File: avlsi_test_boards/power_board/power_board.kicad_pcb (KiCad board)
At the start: 4 copper layers, 99.9 x 100 mm, 100 parts, among them J1 2171750001, J2 2171750001, J3 Conn_01x02_Pin, J4 Conn_01x02_Pin, J5 Conn_01x02_Pin, J6 Conn_01x02_Pin, U1 TLV75709PDBV, U10 TLV1117LV33DCYR, U13 SN74LVC16T245DLR, U14 SN74LVC16T245DLR, U15 SN74LVC16T245DLR, U16 SN74LVC16T245DLR, U17 SN74LVC16T245DLR, U18 SN74LVC16T245DLR, U2 TLV1117LV18DCYR, U3 TLV1117LV25DCYR, U4 TLV1117LV33DCYR, U5 DS04-254-2-04BK-SMT, U6 74HC4051D_653, U7 TLV1117LV18DCYR, U8 TLV75709PDBV, U9 TLV1117LV25DCYR

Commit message: Add production files
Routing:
- net DGND: track 100.2 -> 383.9 mm, vias 92 -> 95
- net DVIN5: track 168.2 -> 171.3 mm, vias 14 -> 12
- net V_Level_Shift: track 88.1 -> 90.4 mm
- net /level_shifters/LS9_DIR1: track 31.3 -> 32.8 mm
- net /level_shifters/LS11_DIR2: track 26.3 -> 25.3 mm
- net MC2_45: track 29.7 -> 28.8 mm
- net MC2_54: track 70.2 -> 70.0 mm, vias 2 -> 1
- net unconnected-(U12B-SYS_CLK_MC2-Pad91): vias 1 -> 0
- net unconnected-(U12B-MC2_73-Pad153): vias 1 -> 0
- net unconnected-(U12B-MC2_71-Pad151): vias 1 -> 0
- net unconnected-(U12B-MC2_69-Pad149): vias 1 -> 0
- net unconnected-(U12B-MC2_67-Pad147): vias 1 -> 0
- net unconnected-(U12B-MC2_65-Pad145): vias 1 -> 0
- net unconnected-(U12B-MC2_63-Pad143): vias 1 -> 0
- net unconnected-(U12B-MC2_61-Pad141): vias 1 -> 0
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
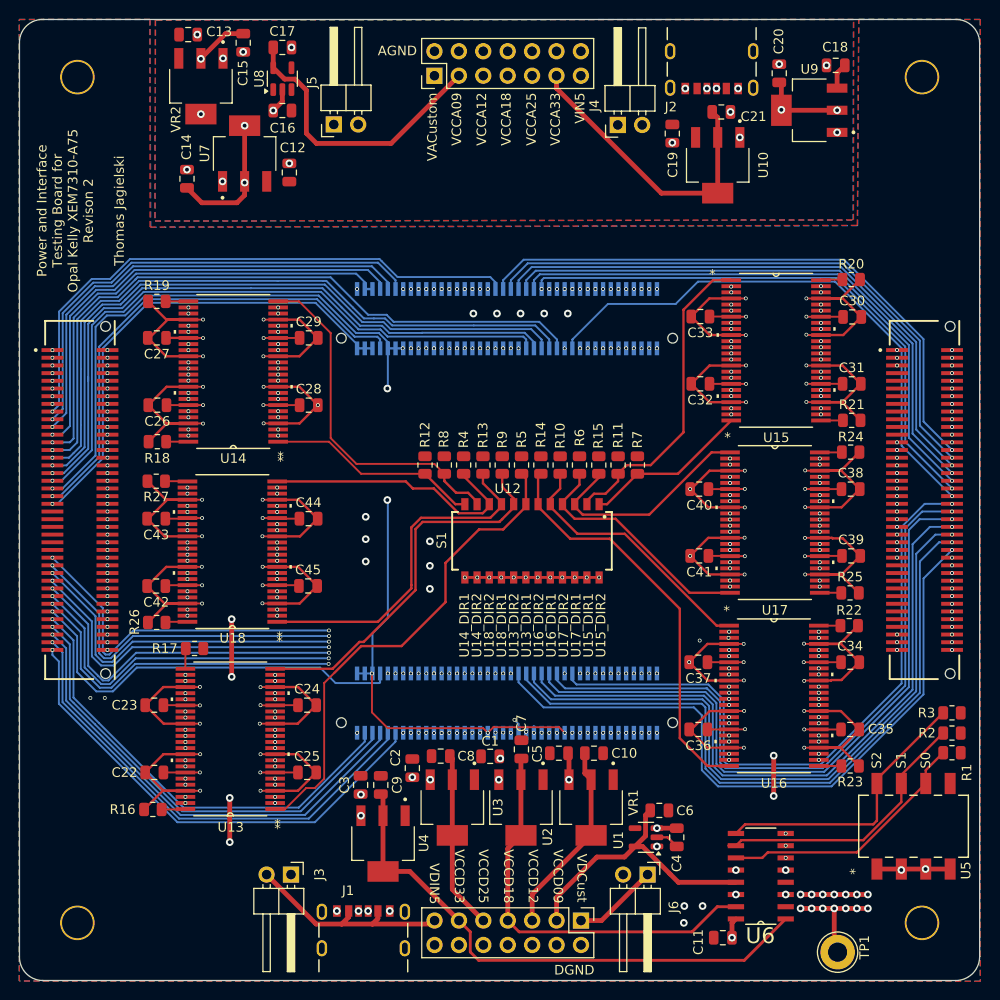
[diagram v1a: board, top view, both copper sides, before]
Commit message: Add power board
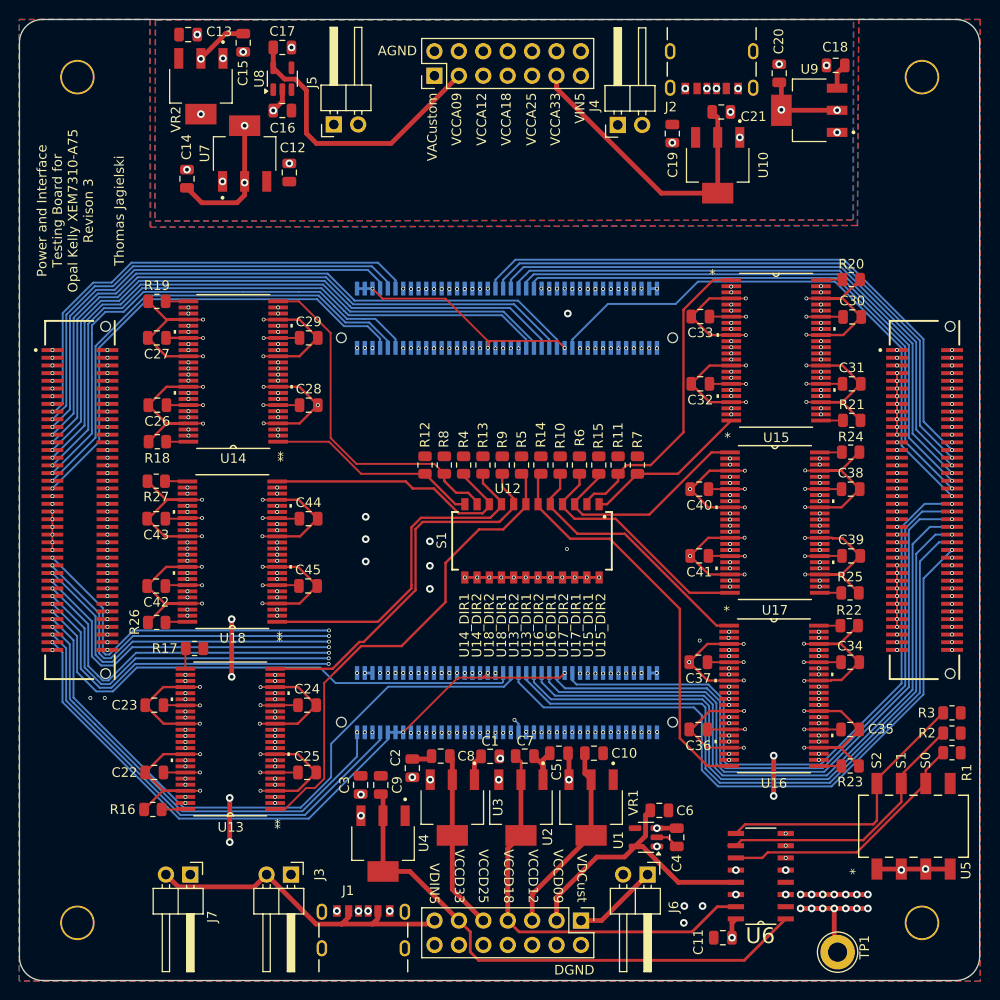
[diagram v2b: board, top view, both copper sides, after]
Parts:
- added J7: Conn_01x02_Pin, Connector_PinHeader_2.54mm:PinHeader_1x02_P2.54mm_Horizontal, F.Cu at (117.9, 114.4)
- moved C7 0.78 mm to (152.7, 102.0), turned to 0 degrees
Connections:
- net MC1_32_PIN renamed MC2_32_PIN
- net MC1_34_PIN renamed MC2_34_PIN
- net MC1_50_PIN renamed MC2_50_PIN
- net MC1_52_PIN renamed MC2_52_PIN
- net MC1_54_PIN renamed MC2_54_PIN
- net MC1_58_PIN renamed MC2_58_PIN
- net MC2_45_PIN renamed MC1_45_PIN
- net MC2_47_PIN renamed MC1_47_PIN
- net MC2_49_PIN renamed MC1_49_PIN
- net MC2_51_PIN renamed MC1_51_PIN
- net MC2_53_PIN renamed MC1_53_PIN
- net MC2_57_PIN renamed MC1_57_PIN
- U12 pad 01: MC1_16_PIN -> MC2_16_PIN
- U12 pad 03: MC1_18_PIN -> MC2_18_PIN
- U12 pad 05: MC1_20_PIN -> MC2_20_PIN
- U12 pad 06: MC1_15_PIN -> MC2_15_PIN
- U12 pad 07: MC1_22_PIN -> MC2_22_PIN
- U12 pad 08: MC1_17_PIN -> MC2_17_PIN
- U12 pad 09: MC1_24_PIN -> MC2_24_PIN
- U12 pad 10: MC1_19_PIN -> MC2_19_PIN
- U12 pad 101: unconnected-(U12B-MC2_21-Pad101) -> DGND
- U12 pad 103: unconnected-(U12B-MC2_23-Pad103) -> DGND
- U12 pad 105: MC1_73_PIN -> MC2_73_PIN
- U12 pad 107: MC1_71_PIN -> MC2_71_PIN
- U12 pad 108: MC1_40 -> MC2_38
- U12 pad 109: MC1_69_PIN -> MC2_69_PIN
- U12 pad 11: MC1_26_PIN -> MC2_26_PIN
- U12 pad 110: MC1_42 -> MC2_40
- U12 pad 111: MC1_67_PIN -> MC2_67_PIN
- U12 pad 112: MC1_44 -> MC2_42
- U12 pad 113: MC1_65_PIN -> MC2_65_PIN
- U12 pad 114: MC1_46 -> MC2_44
- U12 pad 115: MC1_63_PIN -> MC2_63_PIN
- U12 pad 116: MC1_48 -> MC2_46
- U12 pad 117: MC1_61_PIN -> MC2_61_PIN
- U12 pad 118: MC1_50 -> MC2_48
- U12 pad 119: MC1_59_PIN -> MC2_59_PIN
- U12 pad 12: MC1_21_PIN -> MC2_21_PIN
- U12 pad 120: MC1_57 -> MC2_57
- U12 pad 121: MC2_60_PIN -> MC1_60_PIN
- U12 pad 122: MC2_58 -> MC1_58
- U12 pad 123: MC2_62_PIN -> MC1_62_PIN
- U12 pad 124: MC2_54 -> MC1_54
- U12 pad 125: MC2_64_PIN -> MC1_64_PIN
- U12 pad 126: MC2_52 -> MC1_52
- U12 pad 127: MC2_66_PIN -> MC1_66_PIN
- U12 pad 128: MC2_50 -> MC1_50
- U12 pad 129: MC2_68_PIN -> MC1_68_PIN
- U12 pad 13: MC1_28_PIN -> MC2_28_PIN
- U12 pad 130: MC2_48 -> MC1_48
- U12 pad 131: MC2_70_PIN -> MC1_70_PIN
- U12 pad 132: MC2_46 -> MC1_46
- U12 pad 133: MC2_72_PIN -> MC1_72_PIN
- U12 pad 134: MC2_44 -> MC1_44
- U12 pad 135: MC2_74_PIN -> MC1_74_PIN
- U12 pad 136: MC2_67_PIN -> MC1_67_PIN
- U12 pad 137: unconnected-(U12B-MC2_57-Pad137) -> DGND
- U12 pad 138: MC2_69_PIN -> MC1_69_PIN
- U12 pad 139: unconnected-(U12B-MC2_59-Pad139) -> DGND
- U12 pad 14: MC1_23_PIN -> MC2_23_PIN
- U12 pad 140: MC2_71_PIN -> MC1_71_PIN
- U12 pad 141: unconnected-(U12B-MC2_61-Pad141) -> DGND
- U12 pad 142: MC2_73_PIN -> MC1_73_PIN
- U12 pad 143: unconnected-(U12B-MC2_63-Pad143) -> DGND
- U12 pad 144: MC2_75_PIN -> MC1_75_PIN
- U12 pad 145: unconnected-(U12B-MC2_65-Pad145) -> DGND
- U12 pad 146: MC2_77_PIN -> MC1_77_PIN
- U12 pad 147: unconnected-(U12B-MC2_67-Pad147) -> DGND
- U12 pad 148: MC2_79_PIN -> MC1_79_PIN
- U12 pad 149: unconnected-(U12B-MC2_69-Pad149) -> DGND
- U12 pad 15: MC1_30_PIN -> MC2_30_PIN
- U12 pad 150: MC2_61_PIN -> MC1_61_PIN
- U12 pad 151: unconnected-(U12B-MC2_71-Pad151) -> DGND
- U12 pad 152: MC2_59_PIN -> MC1_59_PIN
- U12 pad 153: unconnected-(U12B-MC2_73-Pad153) -> DGND
- U12 pad 155: MC2_76_PIN -> MC1_76_PIN
- U12 pad 157: MC2_63_PIN -> MC1_63_PIN
- U12 pad 159: MC2_65_PIN -> MC1_65_PIN
- U12 pad 16: MC1_25_PIN -> MC2_25_PIN
- U12 pad 17: MC1_38 -> MC2_12
- U12 pad 18: MC1_27_PIN -> MC2_27_PIN
- U12 pad 19: XADC_VP -> MC2_10
- U12 pad 20: MC1_29_PIN -> MC2_29_PIN
- U12 pad 21: XADC_VN -> FPGA_TDO
- U12 pad 22: MC1_31_PIN -> MC2_31_PIN
- U12 pad 23: SYS_CLK_MC1 -> MC2_53
- U12 pad 24: MC1_33_PIN -> MC2_33_PIN
- U12 pad 25: FPGA_10VDD -> MC2_51
- U12 pad 26: MC1_37_PIN -> MC2_37_PIN
- U12 pad 27: MC1_53 -> MC2_49
- U12 pad 28: MC1_39_PIN -> MC2_39_PIN
- U12 pad 29: MC1_51 -> MC2_47
- U12 pad 30: MC1_41_PIN -> MC2_41_PIN
- U12 pad 31: MC1_49 -> MC2_45
- U12 pad 32: MC1_43_PIN -> MC2_43_PIN
- U12 pad 33: MC1_47 -> SYS_CLK_MC2
- U12 pad 34: MC2_26_PIN -> MC1_30_PIN
- U12 pad 35: MC1_45 -> FPGA_TDI
- U12 pad 36: MC2_24_PIN -> MC1_28_PIN
- U12 pad 37: FPGA_33VDD -> FPGA_TMS
- U12 pad 38: MC2_22_PIN -> MC1_26_PIN
- U12 pad 39: FPGA_18VDD -> FPGA_TCK
- U12 pad 40: MC2_20_PIN -> MC1_24_PIN
- U12 pad 41: FPGA_VCDIN -> VCCBATT
- U12 pad 42: MC2_18_PIN -> MC1_22_PIN
- U12 pad 43: unconnected-(U12A-MC1_43-Pad43) -> DGND
- U12 pad 44: MC2_16_PIN -> MC1_20_PIN
- U12 pad 45: unconnected-(U12A-MC1_45-Pad45) -> DGND
- U12 pad 46: MC2_12_PIN -> MC1_18_PIN
- U12 pad 47: unconnected-(U12A-MC1_47-Pad47) -> DGND
- U12 pad 48: MC2_10_PIN -> MC1_16_PIN
- U12 pad 49: unconnected-(U12A-MC1_49-Pad49) -> DGND
- U12 pad 51: unconnected-(U12A-MC1_51-Pad51) -> DGND
- U12 pad 53: unconnected-(U12A-MC1_53-Pad53) -> DGND
- U12 pad 54: MC2_43_PIN -> MC1_43_PIN
- U12 pad 55: MC2_42 -> MC1_38
- U12 pad 56: MC2_41_PIN -> MC1_41_PIN
- U12 pad 57: MC2_40 -> MC1_34
- U12 pad 58: MC2_39_PIN -> MC1_39_PIN
- U12 pad 59: MC2_38 -> MC1_32
- U12 pad 60: MC2_37_PIN -> MC1_37_PIN
- U12 pad 61: MC2_34 -> XADC_VP
- U12 pad 62: MC2_33_PIN -> MC1_33_PIN
- U12 pad 63: MC2_32 -> XADC_VN
- U12 pad 64: MC2_31_PIN -> MC1_31_PIN
- U12 pad 65: MC2_30 -> SYS_CLK_MC1
- U12 pad 66: MC2_15_PIN -> MC1_15_PIN
- U12 pad 67: MC2_28 -> FPGA_10VDD
- U12 pad 68: MC2_17_PIN -> MC1_17_PIN
- U12 pad 69: FPGA_TDO -> MC1_40
- U12 pad 70: MC2_19_PIN -> MC1_19_PIN
- U12 pad 71: VCCBATT -> MC1_42
- U12 pad 72: MC2_21_PIN -> MC1_21_PIN
- U12 pad 73: FPGA_TCK -> FPGA_VCDIN
- U12 pad 74: MC2_23_PIN -> MC1_23_PIN
- U12 pad 75: FPGA_TMS -> FPGA_18VDD
- U12 pad 76: MC2_25_PIN -> MC1_25_PIN
- U12 pad 77: FPGA_TDI -> FPGA_33VDD
- U12 pad 78: MC2_27_PIN -> MC1_27_PIN
- U12 pad 79: SYS_CLK_MC2 -> DGND
- U12 pad 80: MC2_29_PIN -> MC1_29_PIN
- U12 pad 81: MC1_79_PIN -> MC2_79_PIN
- U12 pad 82: MC1_68_PIN -> MC2_68_PIN
- U12 pad 83: MC1_77_PIN -> MC2_77_PIN
- U12 pad 84: MC1_70_PIN -> MC2_70_PIN
- U12 pad 85: MC1_75_PIN -> MC2_75_PIN
- U12 pad 86: MC1_72_PIN -> MC2_72_PIN
- U12 pad 87: unconnected-(U12B-FPGA_TMS-Pad87) -> DGND
- U12 pad 88: MC1_76_PIN -> MC2_76_PIN
- U12 pad 89: unconnected-(U12B-FPGA_TDI-Pad89) -> DGND
- U12 pad 90: MC1_74_PIN -> MC2_74_PIN
- U12 pad 91: unconnected-(U12B-SYS_CLK_MC2-Pad91) -> DGND
- U12 pad 92: MC1_66_PIN -> MC2_66_PIN
- U12 pad 93: unconnected-(U12B-DGND-Pad93) -> DGND
- U12 pad 94: MC1_64_PIN -> MC2_64_PIN
- U12 pad 95: unconnected-(U12B-MC2_15-Pad95) -> DGND
- U12 pad 96: MC1_62_PIN -> MC2_62_PIN
- U12 pad 97: unconnected-(U12B-MC2_17-Pad97) -> DGND
- U12 pad 98: MC1_60_PIN -> MC2_60_PIN
- U12 pad 99: unconnected-(U12B-MC2_19-Pad99) -> DGND
- U13 pad 11: MC2_17 -> MC1_17
- U13 pad 12: MC2_15 -> MC1_15
- U13 pad 13: MC2_31 -> MC1_31
- U13 pad 14: MC2_33 -> MC1_33
- U13 pad 16: MC2_37 -> MC1_37
- U13 pad 17: MC2_39 -> MC1_39
- U13 pad 19: MC2_41 -> MC1_41
- U13 pad 2: MC2_29 -> MC1_29
- U13 pad 20: MC2_43 -> MC1_43
- U13 pad 22: MC2_45 -> MC1_45
- U13 pad 23: MC2_47 -> MC1_47
- U13 pad 29: MC2_43_PIN -> MC1_43_PIN
- U13 pad 3: MC2_27 -> MC1_27
- U13 pad 30: MC2_41_PIN -> MC1_41_PIN
- U13 pad 32: MC2_39_PIN -> MC1_39_PIN
- U13 pad 33: MC2_37_PIN -> MC1_37_PIN
- U13 pad 35: MC2_33_PIN -> MC1_33_PIN
- U13 pad 36: MC2_31_PIN -> MC1_31_PIN
- U13 pad 37: MC2_15_PIN -> MC1_15_PIN
- U13 pad 38: MC2_17_PIN -> MC1_17_PIN
- U13 pad 40: MC2_19_PIN -> MC1_19_PIN
- U13 pad 41: MC2_21_PIN -> MC1_21_PIN
- U13 pad 43: MC2_23_PIN -> MC1_23_PIN
- U13 pad 44: MC2_25_PIN -> MC1_25_PIN
- U13 pad 46: MC2_27_PIN -> MC1_27_PIN
- U13 pad 47: MC2_29_PIN -> MC1_29_PIN
- U13 pad 5: MC2_25 -> MC1_25
- U13 pad 6: MC2_23 -> MC1_23
- U13 pad 8: MC2_21 -> MC1_21
- U13 pad 9: MC2_19 -> MC1_19
- U14 pad 11: MC1_34 -> MC2_34
- U14 pad 12: MC1_32 -> MC2_32
- U14 pad 13: MC1_30 -> MC2_30
- U14 pad 14: MC1_28 -> MC2_28
- U14 pad 16: MC1_26 -> MC2_26
- U14 pad 17: MC1_24 -> MC2_24
- U14 pad 19: MC1_22 -> MC2_22
- U14 pad 2: MC1_25 -> MC2_25
- U14 pad 20: MC1_20 -> MC2_20
- U14 pad 22: MC1_18 -> MC2_18
- U14 pad 23: MC1_16 -> MC2_16
- U14 pad 26: MC1_16_PIN -> MC2_16_PIN
- U14 pad 27: MC1_18_PIN -> MC2_18_PIN
- U14 pad 29: MC1_20_PIN -> MC2_20_PIN
- U14 pad 3: MC1_23 -> MC2_23
- U14 pad 30: MC1_22_PIN -> MC2_22_PIN
- U14 pad 32: MC1_24_PIN -> MC2_24_PIN
- U14 pad 33: MC1_26_PIN -> MC2_26_PIN
- U14 pad 35: MC1_28_PIN -> MC2_28_PIN
- U14 pad 36: MC1_30_PIN -> MC2_30_PIN
- U14 pad 40: MC1_15_PIN -> MC2_15_PIN
- U14 pad 41: MC1_17_PIN -> MC2_17_PIN
- U14 pad 43: MC1_19_PIN -> MC2_19_PIN
- U14 pad 44: MC1_21_PIN -> MC2_21_PIN
- U14 pad 46: MC1_23_PIN -> MC2_23_PIN
- U14 pad 47: MC1_25_PIN -> MC2_25_PIN
- U14 pad 5: MC1_21 -> MC2_21
- U14 pad 6: MC1_19 -> MC2_19
- U14 pad 8: MC1_17 -> MC2_17
- U14 pad 9: MC1_15 -> MC2_15
- U15 pad 11: MC1_64 -> MC2_64
- U15 pad 12: MC1_62 -> MC2_62
- U15 pad 13: MC1_60 -> MC2_60
- U15 pad 14: MC1_58 -> MC2_58
- U15 pad 16: MC1_54 -> MC2_54
- U15 pad 17: MC1_52 -> MC2_52
- U15 pad 19: MC1_50 -> MC2_50
- U15 pad 2: MC1_74 -> MC2_74
- U15 pad 20: MC1_79 -> MC2_79
- U15 pad 22: MC1_77 -> MC2_77
- U15 pad 23: MC1_75 -> MC2_75
- U15 pad 26: MC1_75_PIN -> MC2_75_PIN
- U15 pad 27: MC1_77_PIN -> MC2_77_PIN
- U15 pad 29: MC1_79_PIN -> MC2_79_PIN
- U15 pad 3: MC1_76 -> MC2_76
- U15 pad 36: MC1_60_PIN -> MC2_60_PIN
- U15 pad 37: MC1_62_PIN -> MC2_62_PIN
- U15 pad 38: MC1_64_PIN -> MC2_64_PIN
- U15 pad 40: MC1_66_PIN -> MC2_66_PIN
- U15 pad 41: MC1_68_PIN -> MC2_68_PIN
- U15 pad 43: MC1_70_PIN -> MC2_70_PIN
- U15 pad 44: MC1_72_PIN -> MC2_72_PIN
- U15 pad 46: MC1_76_PIN -> MC2_76_PIN
- U15 pad 47: MC1_74_PIN -> MC2_74_PIN
- U15 pad 5: MC1_72 -> MC2_72
- U15 pad 6: MC1_70 -> MC2_70
- U15 pad 8: MC1_68 -> MC2_68
- U15 pad 9: MC1_66 -> MC2_66
- U16 pad 11: MC2_73 -> MC1_73
- U16 pad 12: MC2_75 -> MC1_75
- U16 pad 13: MC2_77 -> MC1_79
- U16 pad 14: MC2_79 -> MC1_77
- U16 pad 16: MC2_61 -> MC1_61
- U16 pad 17: MC2_59 -> MC1_59
- U16 pad 19: MC2_57 -> MC1_57
- U16 pad 2: MC2_76 -> MC1_76
- U16 pad 20: MC2_53 -> MC1_53
- U16 pad 22: MC2_51 -> MC1_51
- U16 pad 23: MC2_49 -> MC1_49
- U16 pad 3: MC2_63 -> MC1_63
- U16 pad 32: MC2_59_PIN -> MC1_59_PIN
- U16 pad 33: MC2_61_PIN -> MC1_61_PIN
- U16 pad 35: MC2_79_PIN -> MC1_79_PIN
- U16 pad 36: MC2_77_PIN -> MC1_77_PIN
- U16 pad 37: MC2_75_PIN -> MC1_75_PIN
- U16 pad 38: MC2_73_PIN -> MC1_73_PIN
- U16 pad 40: MC2_71_PIN -> MC1_71_PIN
- U16 pad 41: MC2_69_PIN -> MC1_69_PIN
- U16 pad 43: MC2_67_PIN -> MC1_67_PIN
- U16 pad 44: MC2_65_PIN -> MC1_65_PIN
- U16 pad 46: MC2_63_PIN -> MC1_63_PIN
- U16 pad 47: MC2_76_PIN -> MC1_76_PIN
- U16 pad 5: MC2_65 -> MC1_65
- U16 pad 6: MC2_67 -> MC1_67
- U16 pad 8: MC2_69 -> MC1_69
- U16 pad 9: MC2_71 -> MC1_71
- U17 pad 11: MC1_61 -> MC2_61
- U17 pad 12: MC1_59 -> MC2_59
- U17 pad 13: MC2_60 -> MC1_60
- U17 pad 14: MC2_62 -> MC1_62
- U17 pad 16: MC2_64 -> MC1_64
- U17 pad 17: MC2_66 -> MC1_66
- U17 pad 19: MC2_68 -> MC1_68
- U17 pad 2: MC1_73 -> MC2_73
- U17 pad 20: MC2_70 -> MC1_70
- U17 pad 22: MC2_72 -> MC1_72
- U17 pad 23: MC2_74 -> MC1_74
- U17 pad 26: MC2_74_PIN -> MC1_74_PIN
- U17 pad 27: MC2_72_PIN -> MC1_72_PIN
- U17 pad 29: MC2_70_PIN -> MC1_70_PIN
- U17 pad 3: MC1_71 -> MC2_71
- U17 pad 30: MC2_68_PIN -> MC1_68_PIN
- U17 pad 32: MC2_66_PIN -> MC1_66_PIN
- U17 pad 33: MC2_64_PIN -> MC1_64_PIN
- U17 pad 35: MC2_62_PIN -> MC1_62_PIN
- U17 pad 36: MC2_60_PIN -> MC1_60_PIN
- U17 pad 37: MC1_59_PIN -> MC2_59_PIN
- U17 pad 38: MC1_61_PIN -> MC2_61_PIN
- U17 pad 40: MC1_63_PIN -> MC2_63_PIN
- U17 pad 41: MC1_65_PIN -> MC2_65_PIN
- U17 pad 43: MC1_67_PIN -> MC2_67_PIN
- U17 pad 44: MC1_69_PIN -> MC2_69_PIN
- U17 pad 46: MC1_71_PIN -> MC2_71_PIN
- U17 pad 47: MC1_73_PIN -> MC2_73_PIN
- U17 pad 5: MC1_69 -> MC2_69
- U17 pad 6: MC1_67 -> MC2_67
- U17 pad 8: MC1_65 -> MC2_65
- U17 pad 9: MC1_63 -> MC2_63
- U18 pad 11: MC2_24 -> MC1_28
- U18 pad 12: MC2_26 -> MC1_30
- U18 pad 13: MC1_43 -> MC2_43
- U18 pad 14: MC1_41 -> MC2_41
- U18 pad 16: MC1_39 -> MC2_39
- U18 pad 17: MC1_37 -> MC2_37
- U18 pad 19: MC1_33 -> MC2_33
- U18 pad 2: MC2_10 -> MC1_16
- U18 pad 20: MC1_31 -> MC2_31
- U18 pad 22: MC1_29 -> MC2_29
- U18 pad 23: MC1_27 -> MC2_27
- U18 pad 26: MC1_27_PIN -> MC2_27_PIN
- U18 pad 27: MC1_29_PIN -> MC2_29_PIN
- U18 pad 29: MC1_31_PIN -> MC2_31_PIN
- U18 pad 3: MC2_12 -> MC1_18
- U18 pad 30: MC1_33_PIN -> MC2_33_PIN
- U18 pad 32: MC1_37_PIN -> MC2_37_PIN
- U18 pad 33: MC1_39_PIN -> MC2_39_PIN
- U18 pad 35: MC1_41_PIN -> MC2_41_PIN
- U18 pad 36: MC1_43_PIN -> MC2_43_PIN
- U18 pad 37: MC2_26_PIN -> MC1_30_PIN
- U18 pad 38: MC2_24_PIN -> MC1_28_PIN
- U18 pad 40: MC2_22_PIN -> MC1_26_PIN
- U18 pad 41: MC2_20_PIN -> MC1_24_PIN
- U18 pad 43: MC2_18_PIN -> MC1_22_PIN
- U18 pad 44: MC2_16_PIN -> MC1_20_PIN
- U18 pad 46: MC2_12_PIN -> MC1_18_PIN
- U18 pad 47: MC2_10_PIN -> MC1_16_PIN
- U18 pad 5: MC2_16 -> MC1_20
- U18 pad 6: MC2_18 -> MC1_22
- U18 pad 8: MC2_20 -> MC1_24
- U18 pad 9: MC2_22 -> MC1_26
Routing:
- net MC1_53: track 71.1 -> 19.1 mm, vias 1 -> 2
- net MC1_51: track 70.4 -> 19.7 mm, vias 1 -> 2
- net MC2_53: track 19.2 -> 69.0 mm, vias 2 -> 1
- net MC1_49: track 69.6 -> 20.7 mm, vias 1 -> 2
- net MC2_58: track 68.4 -> 19.6 mm, vias 1 -> 2
- net MC1_58: track 19.6 -> 68.4 mm, vias 2 -> 1
- net MC2_51: track 19.6 -> 68.4 mm, vias 2 -> 1
- net MC1_54: track 22.1 -> 70.0 mm, vias 2 -> 1
- net MC2_54: track 70.0 -> 22.1 mm, vias 1 -> 2
- net MC2_52: track 70.9 -> 23.2 mm, vias 1 -> 2
- net MC1_52: track 23.2 -> 70.9 mm, vias 2 -> 1
- net MC2_49: track 20.7 -> 67.8 mm, vias 2 -> 1
- net MC2_50: track 71.0 -> 25.1 mm, vias 1 -> 2
- net MC2_57: track 17.4 -> 58.1 mm, vias 2 -> 1
- net MC1_57: track 58.1 -> 17.5 mm, vias 1 -> 2
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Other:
- board text added: "FPGAVIN"
- board text added: "Power and Interface Testing Board for Opal Kelly XEM7310-A75 Revison 3 Thomas Jagielski"
- board text removed: "Power and Interface Testing Board for Opal Kelly XEM7310-A75 Revison 2 Thomas Jagielski"
